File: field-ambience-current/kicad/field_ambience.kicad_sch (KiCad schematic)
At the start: 0 parts

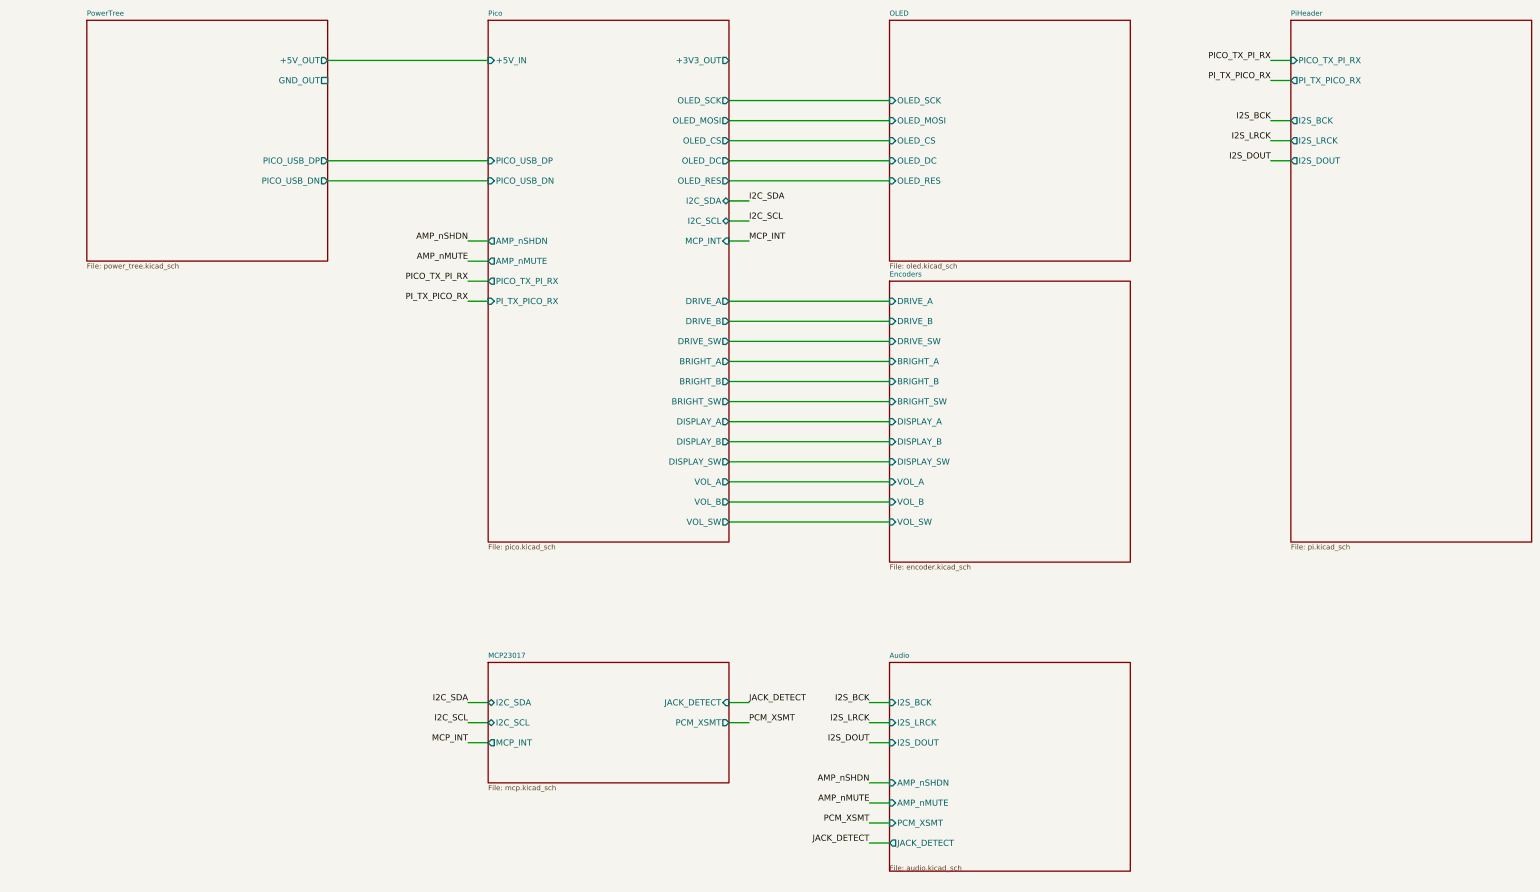
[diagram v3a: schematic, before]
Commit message: feat(native): Step 6 — Pi removed from schematic + BOM (97→92 parts)
Now that the RP2350 owns display, buttons, encoders, and I²S audio
(Steps 1-5), the Raspberry Pi Zero 2 W comes out of the device.

generate_kicad_project.py:
- Deleted pi.kicad_sch (Sheet 7, Pi header); removed it from the kicad_pro
  sheet list, the root sheet hierarchy, and main()'s writer.
- 5 components removed: J2 (40-pin Pi header), R1 (UART RX series),
  R_BCK/R_LRCK/R_DOUT (Pi-side I²S series Rs). Real component count 97→92.
- pico_sheet: GP0/GP1/GP4 repurposed from UART TX/RX + unused OLED MISO
  to I2S_BCK / I2S_LRCK / I2S_DOUT (RP2350 PIO I²S master). Fixed a
  pin-number vs GP-number slip so I2C_SDA/SCL stay on pins 4/5.
- root_sheet: Pico symbol's 2 UART pins replaced with 3 I²S output pins;
  UART + Pi-side label bridges removed; new Pico-I²S→Audio label bridges
  added (audio-side I²S labels were already present, now Pico-driven).
- D2 (TVS) kept: it sits on the +5V main rail, not the Pi header — stays
  as general rail surge protection.

Verification:
- Regenerates clean; pi.kicad_sch not recreated; all sheets paren-balanced.
- Removed nets (PICO_TX_PI_RX/PI_TX_PICO_RX/OLED_MISO_NC) gone everywhere.
- I²S nets continuous pico→root→audio; every pico hier-label has a root pin
  (only ADC_VREF_NC unmatched — pre-existing intentional NC).
- kicad-happy analyzer: 6 VM-001 blockers, ALL the documented false-positive
  class (Pico VBUS pin makes the heuristic treat GPIOs as 5V; real I²S is
  GP0/1/4 @ 3V3 → PCM5102A @ 3V3, no level shifter needed). Warnings 19→16.
  GUI ERC (B3) remains the authority.

Docs: SPEC §5 pin rows + v0.9 banner, CHANGELOG v0.9, MEINE_TODO Abschnitt 0,
NATIVE_PORT_PLAN Step 6 ticked + D2 correction. pi_sheet() left as dead code
(uncalled) to keep the diff focused.

https://claude.ai/code/session_01K5kLTFpDCCoYwx2dq6RkAv
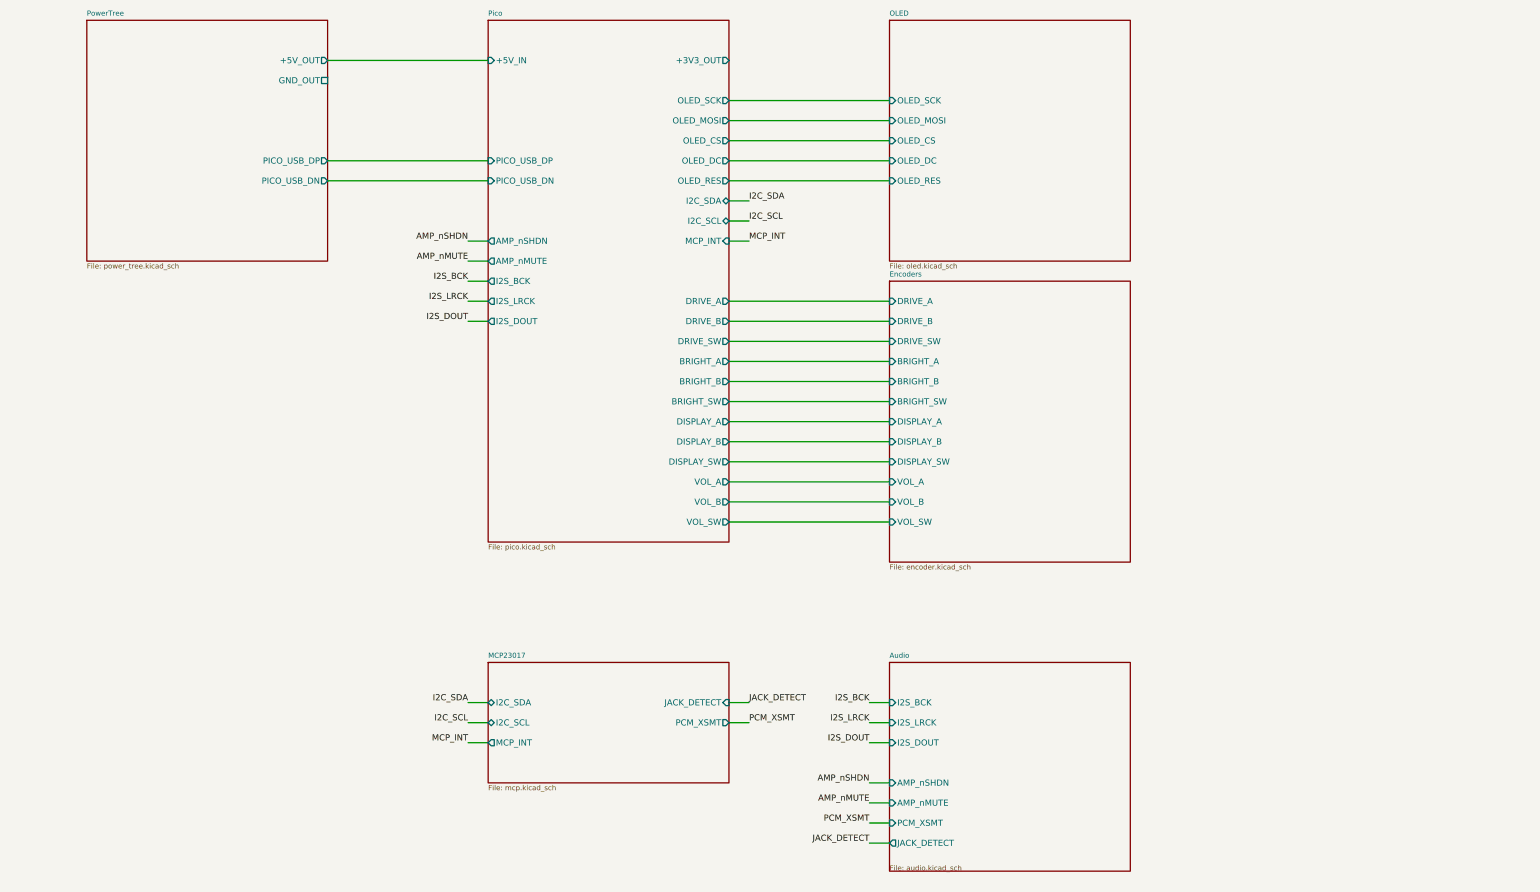
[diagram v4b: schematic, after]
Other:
- removed sheet PiHeader
- sheet Pico ports: added I2S_BCK, I2S_DOUT, I2S_LRCK; removed PICO_TX_PI_RX, PI_TX_PICO_RX
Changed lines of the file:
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@@
       (effects (font (size 1.524 1.524)) (justify left))
 )
-    (pin "PICO_TX_PI_RX" output (at 130 105 180)
+    (pin "I2S_BCK" output (at 130 105 180)
       (effects (font (size 1.524 1.524)) (justify left))
 )
-    (pin "PI_TX_PICO_RX" input (at 130 110 180)
+    (pin "I2S_LRCK" output (at 130 110 180)
+      (effects (font (size 1.524 1.524)) (justify left))
+)
+    (pin "I2S_DOUT" output (at 130 115 180)
       (effects (font (size 1.524 1.524)) (justify left))
 ))
@@
   (wire (pts (xy 125 220) (xy 130 220)) (stroke (width 0) (type default)))
   (label "MCP_INT" (at 125 220 0) (effects (font (size 1.524 1.524)) (justify right bottom)))
-  (sheet (at 330 40) (size 60 130) (fields_autoplaced)
-    (stroke (width 0.1524) (type solid))
-    (fill (color 0 0 0 0.0000))
-    (property "Sheetname" "PiHeader" (at 330 39 0)
-      (effects (font (size 1.27 1.27)) (justify left bottom)))
-    (property "Sheetfile" "pi.kicad_sch" (at 330 170.5 0)
-      (effects (font (size 1.27 1.27)) (justify left top)))
-    (pin "PICO_TX_PI_RX" input (at 330 50 180)
-      (effects (font (size 1.524 1.524)) (justify left))
-)
-    (pin "PI_TX_PICO_RX" output (at 330 55 180)
-      (effects (font (size 1.524 1.524)) (justify left))
-)
-    (pin "I2S_BCK" output (at 330 65 180)
-      (effects (font (size 1.524 1.524)) (justify left))
-)
-    (pin "I2S_LRCK" output (at 330 70 180)
-      (effects (font (size 1.524 1.524)) (justify left))
-)
-    (pin "I2S_DOUT" output (at 330 75 180)
-      (effects (font (size 1.524 1.524)) (justify left))
-))
   (wire (pts (xy 125 105) (xy 130 105)) (stroke (width 0) (type default)))
-  (label "PICO_TX_PI_RX" (at 125 105 0) (effects (font (size 1.524 1.524)) (justify right bottom)))
+  (label "I2S_BCK" (at 125 105 0) (effects (font (size 1.524 1.524)) (justify right bottom)))
   (wire (pts (xy 125 110) (xy 130 110)) (stroke (width 0) (type default)))
-  (label "PI_TX_PICO_RX" (at 125 110 0) (effects (font (size 1.524 1.524)) (justify right bottom)))
-  (wire (pts (xy 325 50) (xy 330 50)) (stroke (width 0) (type default)))
-  (label "PICO_TX_PI_RX" (at 325 50 0) (effects (font (size 1.524 1.524)) (justify right bottom)))
-  (wire (pts (xy 325 55) (xy 330 55)) (stroke (width 0) (type default)))
-  (label "PI_TX_PICO_RX" (at 325 55 0) (effects (font (size 1.524 1.524)) (justify right bottom)))
-  (wire (pts (xy 325 65) (xy 330 65)) (stroke (width 0) (type default)))
-  (label "I2S_BCK" (at 325 65 0) (effects (font (size 1.524 1.524)) (justify right bottom)))
-  (wire (pts (xy 325 70) (xy 330 70)) (stroke (width 0) (type default)))
-  (label "I2S_LRCK" (at 325 70 0) (effects (font (size 1.524 1.524)) (justify right bottom)))
-  (wire (pts (xy 325 75) (xy 330 75)) (stroke (width 0) (type default)))
-  (label "I2S_DOUT" (at 325 75 0) (effects (font (size 1.524 1.524)) (justify right bottom)))
+  (label "I2S_LRCK" (at 125 110 0) (effects (font (size 1.524 1.524)) (justify right bottom)))
+  (wire (pts (xy 125 115) (xy 130 115)) (stroke (width 0) (type default)))
+  (label "I2S_DOUT" (at 125 115 0) (effects (font (size 1.524 1.524)) (justify right bottom)))
   (sheet (at 230 200) (size 60 52) (fields_autoplaced)
     (stroke (width 0.1524) (type solid))
